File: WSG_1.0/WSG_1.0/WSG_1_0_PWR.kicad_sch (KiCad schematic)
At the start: 42 parts, among them J2 USB_C_Receptacle_USB2.0_16P, J4 Conn_01x02, U10 TPS22916CYFPR, U11 W25N02KVZEIR, U12 USBLC6-2SC6, U7 BQ25180YBGR, U8 TPS63802DLAR, U9 TPS7A2025PDBVR

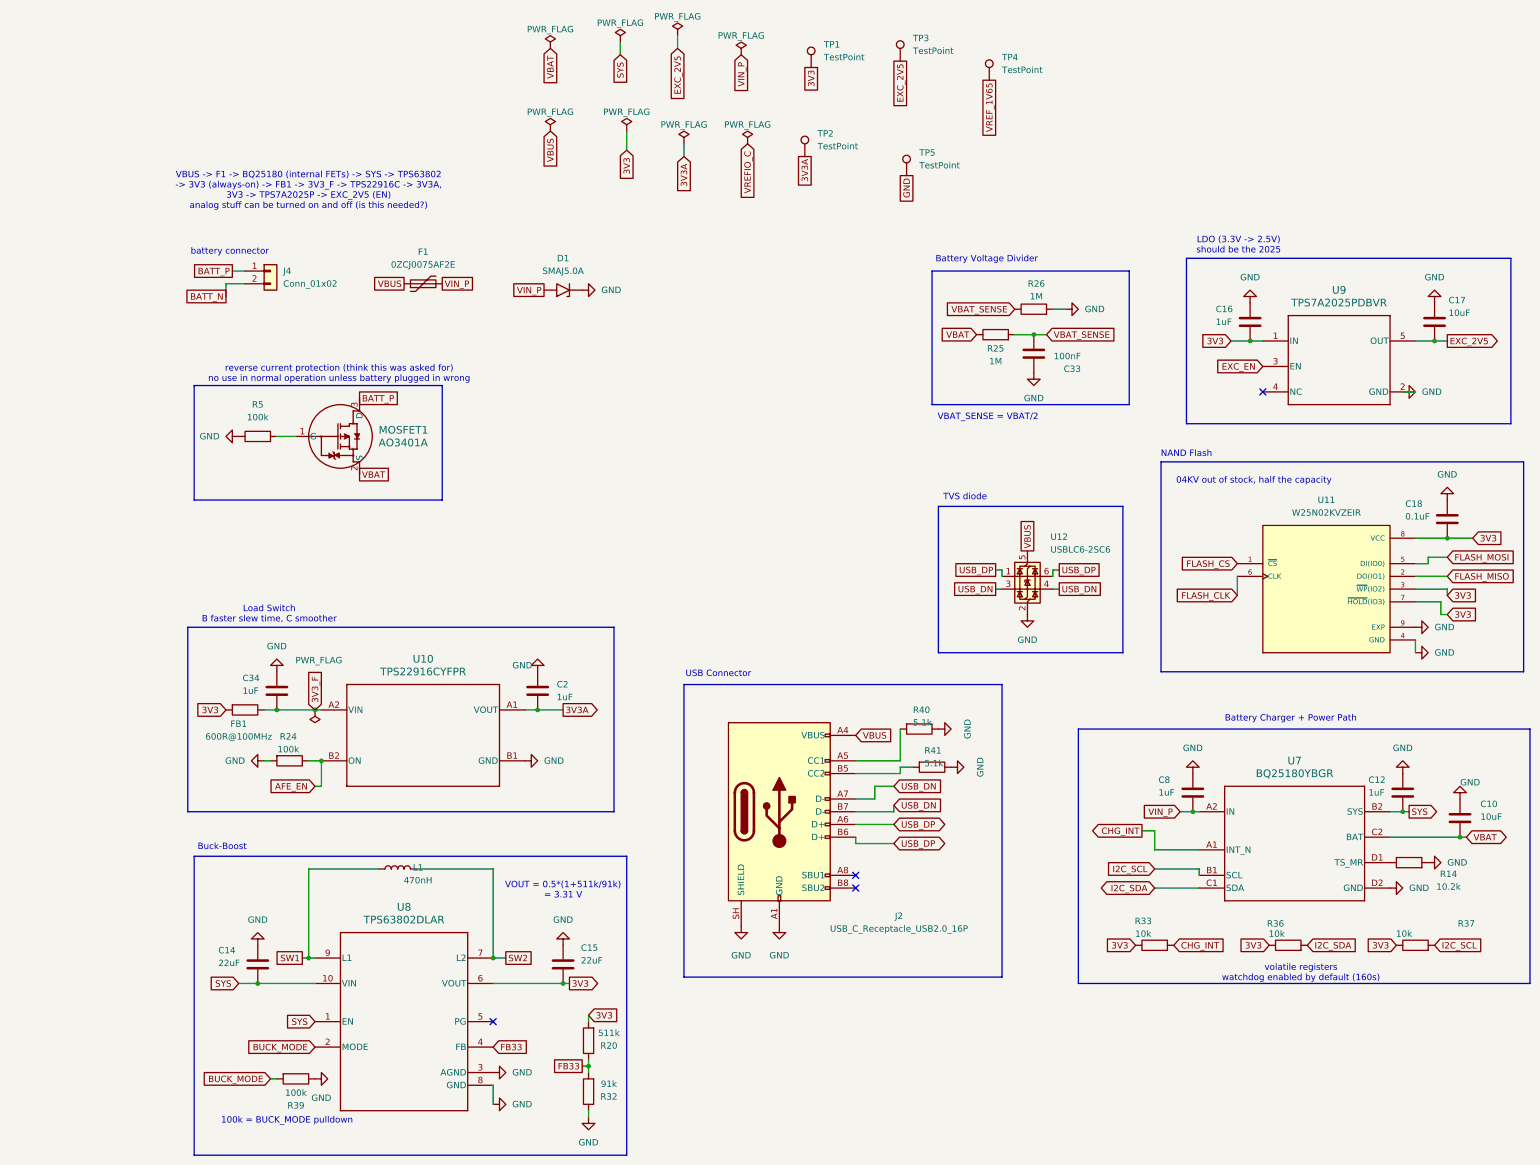
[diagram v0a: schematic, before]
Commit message: labeled schematic flags, now doing routing stuff
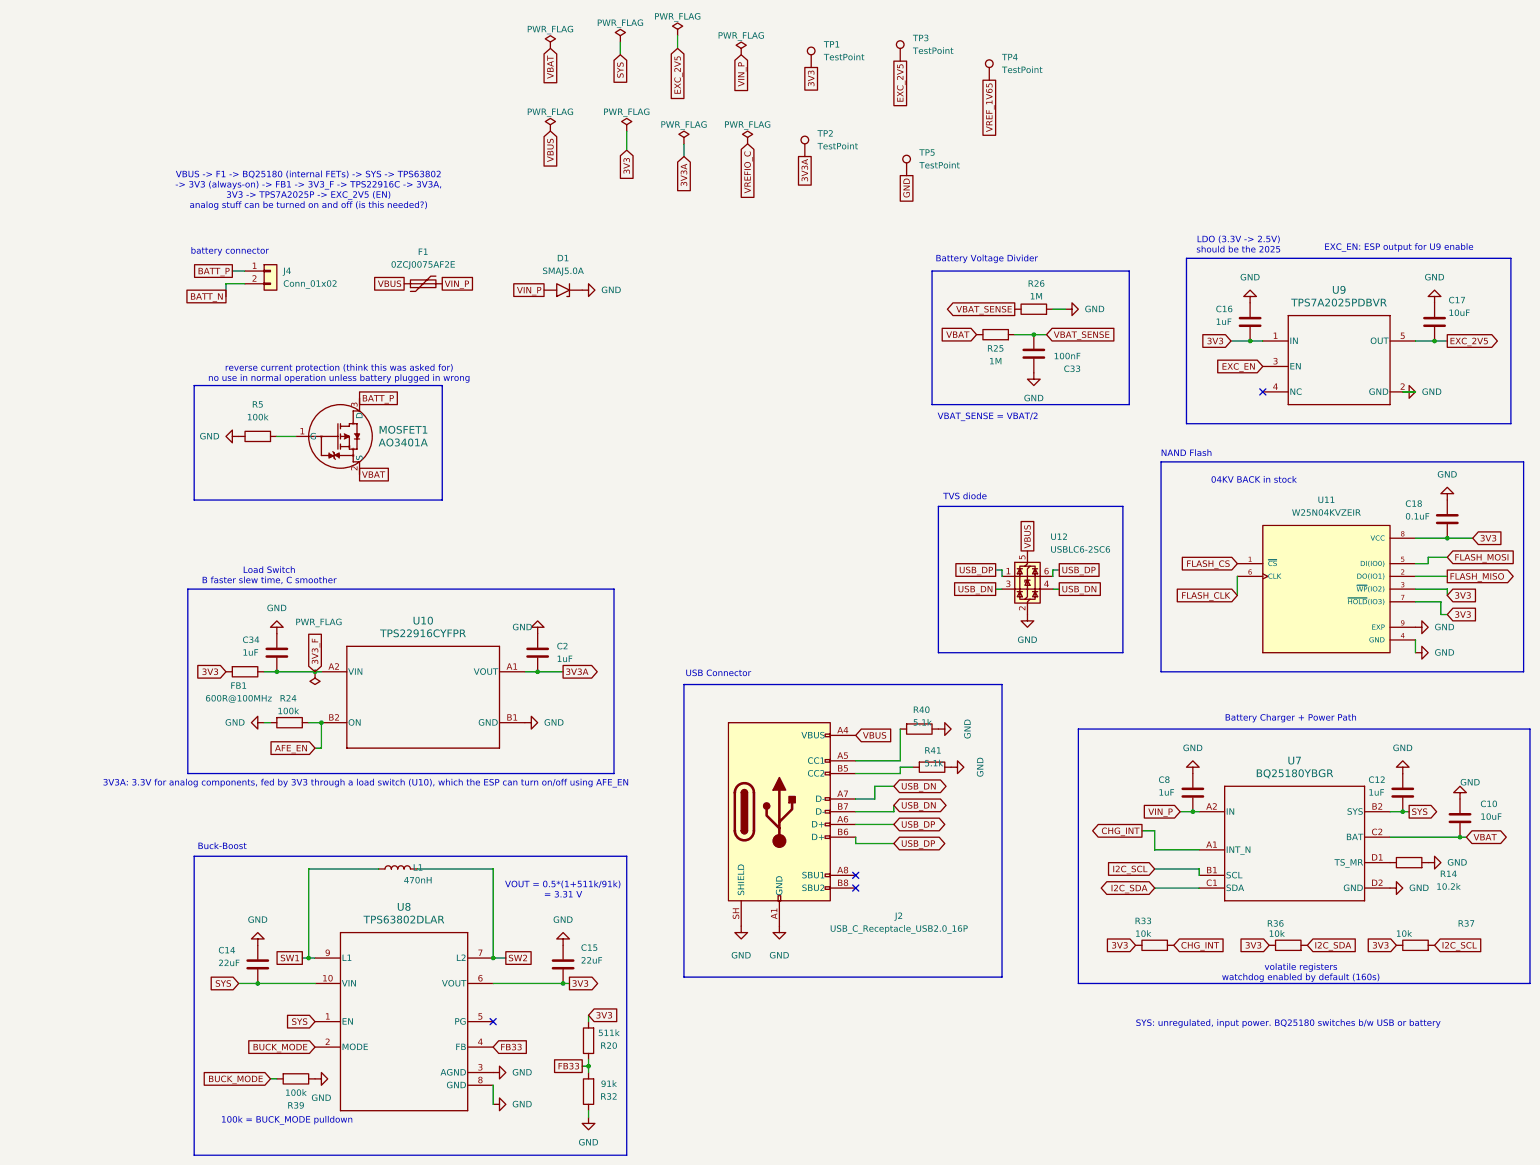
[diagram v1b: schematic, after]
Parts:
- U11: value W25N02KVZEIR -> W25N04KVZEIR; MP W25N02KVZEIR -> W25N04KVZEIR
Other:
- note added: "04KV BACK in stock"
- note added: "3V3A: 3.3V for analog components, fed by 3V3 through a load switch (U10), which the ESP can turn on/off using AFE_EN"
- note added: "EXC_EN: ESP output for U9 enable"
- note added: "SYS: unregulated, input power. BQ25180 switches b/w USB or battery"
- note removed: "04KV out of stock, half the capacity"
- moved on the sheet: C2, C34, FB1, R24, U10

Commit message: adding connectors, ordering stuff
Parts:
- TP1, TP2, TP3, TP4, TP5: now left out of the parts list
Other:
- note added: "SYS: unregulated, input power. BQ25180 output that switches b/w USB or battery"
- note added: "volatile registers"
- note removed: "SYS: unregulated, input power. BQ25180 switches b/w USB or battery"
- note removed: "volatile registers watchdog enabled by default (160s)"
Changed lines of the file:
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@@
 		)
 	)
-	(text "volatile registers\nwatchdog enabled by default (160s)"
+	(text "volatile registers"
 		(exclude_from_sim no)
 		(at 237.49 159.258 0)
@@
 		)
 	)
-	(text "SYS: unregulated, input power. BQ25180 switches b/w USB or battery"
+	(text "SYS: unregulated, input power. BQ25180 output that switches b/w USB or battery"
 		(exclude_from_sim no)
 		(at 234.95 169.418 0)
@@
 		(body_style 1)
 		(exclude_from_sim no)
-		(in_bom yes)
+		(in_bom no)
 		(on_board yes)
-		(in_pos_files yes)
+		(in_pos_files no)
 		(dnp no)
 		(fields_autoplaced yes)
@@
 		(body_style 1)
 		(exclude_from_sim no)
-		(in_bom yes)
+		(in_bom no)
 		(on_board yes)
-		(in_pos_files yes)
+		(in_pos_files no)
 		(dnp no)
 		(fields_autoplaced yes)
@@
 		(body_style 1)
 		(exclude_from_sim no)
-		(in_bom yes)
+		(in_bom no)
 		(on_board yes)
-		(in_pos_files yes)
+		(in_pos_files no)
 		(dnp no)
 		(fields_autoplaced yes)
@@
 		(body_style 1)
 		(exclude_from_sim no)
-		(in_bom yes)
+		(in_bom no)
 		(on_board yes)
-		(in_pos_files yes)
+		(in_pos_files no)
 		(dnp no)
 		(fields_autoplaced yes)
@@
 		(body_style 1)
 		(exclude_from_sim no)
-		(in_bom yes)
+		(in_bom no)
 		(on_board yes)
-		(in_pos_files yes)
+		(in_pos_files no)
 		(dnp no)
 		(fields_autoplaced yes)

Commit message: schematic changes finished?
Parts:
- removed MOSFET1: AO3401A, Package_TO_SOT_SMD:SOT-23, symbol dmp2035u7:DMP2035U-7
- removed R5: 100k, Resistor_SMD:R_0402_1005Metric_Pad0.72x0.64mm_HandSolder, symbol Device:R
- added C19: 1uF, Capacitor_SMD:C_0402_1005Metric_Pad0.74x0.62mm_HandSolder, symbol Device:C
- C12: value 1uF -> 10uF
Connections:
- net 3V3: now also C19.2; no longer C16.2, U9.1 (IN)
- net 3V3A: now also C16.2, U9.1 (IN)
- net GND: now also D1.2 (A2), C19.1; no longer D1.1 (A1)
- net VIN_P: now also D1.1 (A1); no longer D1.2 (A2)
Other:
- moved on the sheet: C18

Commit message: got rid of pfet, added bypass for tps (u10)
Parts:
- added R59: 0, Resistor_SMD:R_0402_1005Metric_Pad0.72x0.64mm_HandSolder, symbol Device:R
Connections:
- net BATT_P is gone; now on net VBAT: J4.1 (Pin_1)
- net 3V3A: now also R59.1
- net 3V3_F: now also R59.2
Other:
- note added: "AFE_EN = IO37, EXC_EN = IO38 - neither is an RTC GPIO. Both float high-Z in deep sleep; R24 and U9's internal EN pulldown default them off. Safe on reset/crash. FIRMWARE: on the normal sleep path, drive EXC_EN low and wait before AFE_EN low. Do not let both float together - U9 can be damaged by reverse current if its input collapses while C17 is still charged."
- note added: "Bypass for U10, only if U10 is depopulated"
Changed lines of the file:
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@@
 		)
 	)
+	(text "AFE_EN = IO37, EXC_EN = IO38 - neither is an RTC GPIO.\nBoth float high-Z in deep sleep; R24 and U9's internal EN pulldown\ndefault them off. Safe on reset/crash.\n\nFIRMWARE: on the normal sleep path, drive EXC_EN low and wait\nbefore AFE_EN low. Do not let both float together - U9 can be\ndamaged by reverse current if its input collapses while C17 is\nstill charged."
+		(exclude_from_sim no)
+		(at 120.396 47.244 0)
+		(effects
+			(font
+				(size 1.27 1.27)
+			)
+		)
+	)
 	(text "Buck-Boost"
 		(exclude_from_sim no)
@@
 		)
 	)
+	(text "Bypass for U10, only if U10 is depopulated"
+		(exclude_from_sim no)
+		(at 65.278 71.882 0)
+		(effects
+			(font
+				(size 1.27 1.27)
+			)
+		)
+	)
 	(text "VOUT = 0.5*(1+511k/91k) \n= 3.31 V \n"
 		(exclude_from_sim no)
@@
 		)
 	)
-	(global_label "BATT_P"
+	(global_label "VBAT"
 		(shape passive)
 		(at 24.13 19.05 180)
@@
 		)
 		(property "Intersheetrefs" "${INTERSHEET_REFS}"
-			(at 15.7247 19.05 0)
+			(at 17.8413 19.05 0)
 			(hide yes)
 			(show_name no)
@@
 		)
 	)
+	(global_label "3V3A"
+		(shape output)
+		(at 67.31 78.74 0)
+		(fields_autoplaced yes)
+		(effects
+			(font
+				(size 1.27 1.27)
+			)
+			(justify left)
+		)
+		(property "Intersheetrefs" "${INTERSHEET_REFS}"
+			(at 74.8914 78.74 0)
+			(hide yes)
+			(show_name no)
+			(do_not_autoplace no)
+			(effects
+				(font
+					(size 1.27 1.27)
+				)
+				(justify left)
+			)
+		)
+	)
 	(global_label "FLASH_CLK"
 		(shape input)
@@
 		)
 	)
+	(global_label "3V3_F"
+		(shape input)
+		(at 59.69 78.74 180)
+		(fields_autoplaced yes)
+		(effects
+			(font
+				(size 1.27 1.27)
+			)
+			(justify right)
+		)
+		(property "Intersheetrefs" "${INTERSHEET_REFS}"
+			(at 51.141 78.74 0)
+			(hide yes)
+			(show_name no)
+			(do_not_autoplace no)
+			(effects
+				(font
+					(size 1.27 1.27)
+				)
+				(justify right)
+			)
+		)
+	)
 	(global_label "3V3"
 		(shape input)
@@
 					(unit 1)
 				)
+			)
+		)
+	)
+	(symbol
+		(lib_id "Device:R")
+		(at 63.5 78.74 270)
+		(unit 1)
+		(body_style 1)
+		(exclude_from_sim no)
+		(in_bom yes)
+		(on_board yes)
+		(in_pos_files yes)
+		(dnp yes)
+		(property "Reference" "R59"
+			(at 63.246 73.914 90)
+			(show_name no)
+			(do_not_autoplace no)
+			(effects
+				(font
+					(size 1.27 1.27)
+				)
+			)
+		)
+		(property "Value" "0"
+			(at 63.246 76.454 90)
+			(show_name no)
+			(do_not_autoplace no)
+			(effects
+				(font
+					(size 1.27 1.27)
+				)
+			)
+		)
+		(property "Footprint" "Resistor_SMD:R_0402_1005Metric_Pad0.72x0.64mm_HandSolder"
+			(at 63.5 76.962 90)
+			(hide yes)
+			(show_name no)
+			(do_not_autoplace no)
+			(effects
+				(font
+					(size 1.27 1.27)
+				)
+			)
+		)
+		(property "Datasheet" ""
+			(at 63.5 78.74 0)
+			(hide yes)
+			(show_name no)
+			(do_not_autoplace no)
+			(effects
+				(font
+					(size 1.27 1.27)
+				)
+			)
+		)
+		(property "Description" "Resistor"
+			(at 63.5 78.74 0)
+			(hide yes)
+			(show_name no)
+			(do_not_autoplace no)
+			(effects
+				(font
+					(size 1.27 1.27)
+				)
+			)
+		)
+		(pin "1"
+		)
+		(pin "2"
+		)
+		(instances
+			(project "WSG_1.0"
+				(path "/cb65811d-b245-4002-a5a3-eef29f2c4ddb/05f78620-165f-4d12-a698-3b5ab7aa33dd"
+					(reference "R59")
+					(unit 1)
+				)

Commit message: production files generated
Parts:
- C14, C15: MPN GRM188R60J226MEA0J -> CL10A226MQ8NRNE
- U9: value TPS7A2025PDBVR -> LP5907MFX-2.5/NOPB
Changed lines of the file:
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@@
 			)
 		)
-		(property "Value" "TPS7A2025PDBVR"
+		(property "Value" "LP5907MFX-2.5/NOPB"
 			(at 245.11 25.4 0)
 			(show_name no)
@@
 			)
 		)
-		(property "MPN" "GRM188R60J226MEA0J"
+		(property "MPN" "CL10A226MQ8NRNE"
 			(at 90.17 157.48 0)
 			(hide yes)
@@
 			)
 		)
-		(property "MPN" "GRM188R60J226MEA0J"
+		(property "MPN" "CL10A226MQ8NRNE"
 			(at 29.21 157.48 0)
 			(hide yes)
